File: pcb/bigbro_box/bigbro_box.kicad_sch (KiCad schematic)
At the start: 31 parts

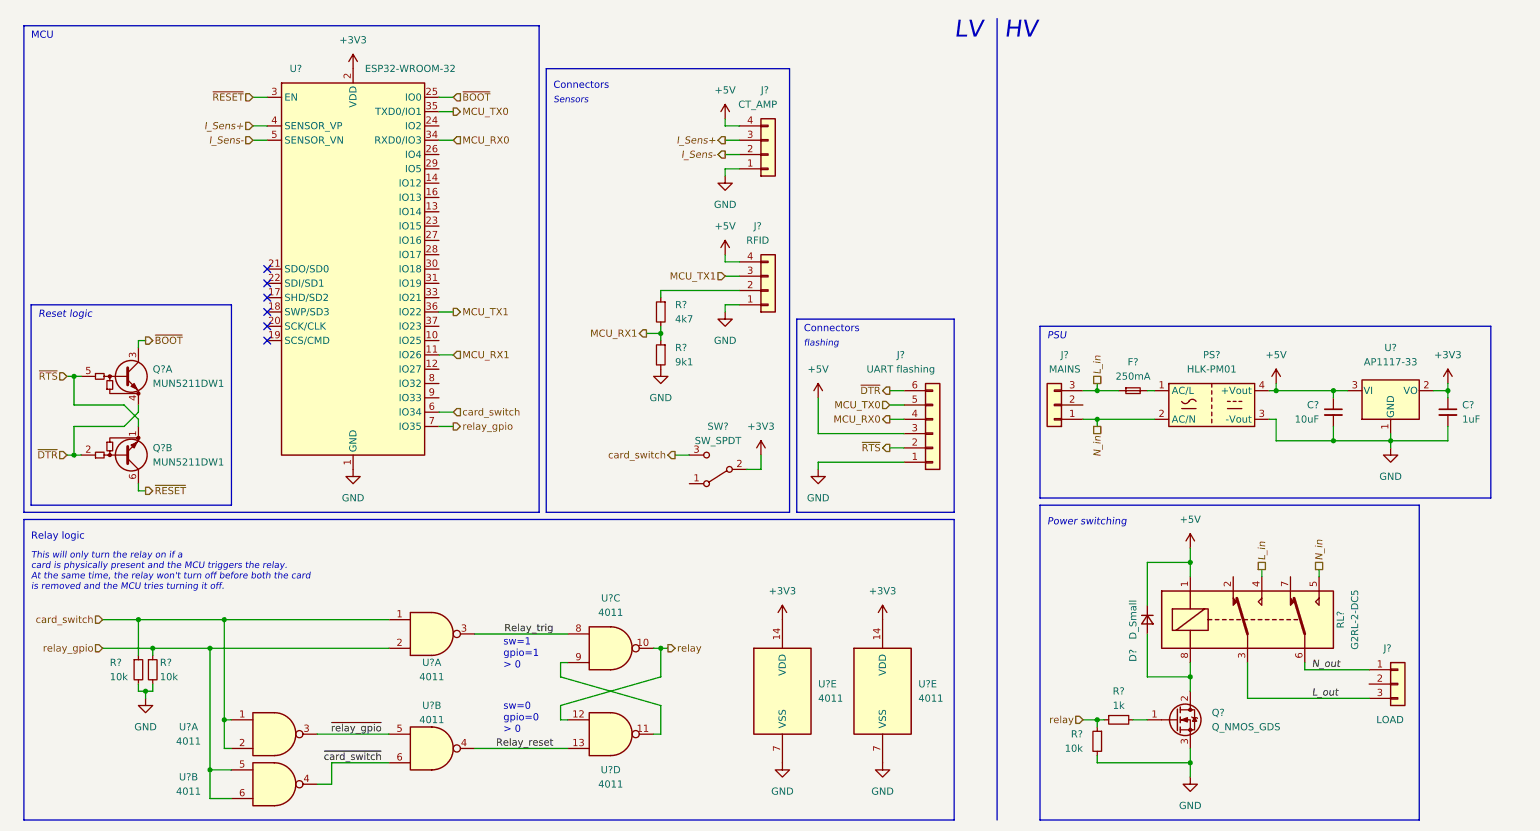
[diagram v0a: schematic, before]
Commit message: Added resistive divider to RX0
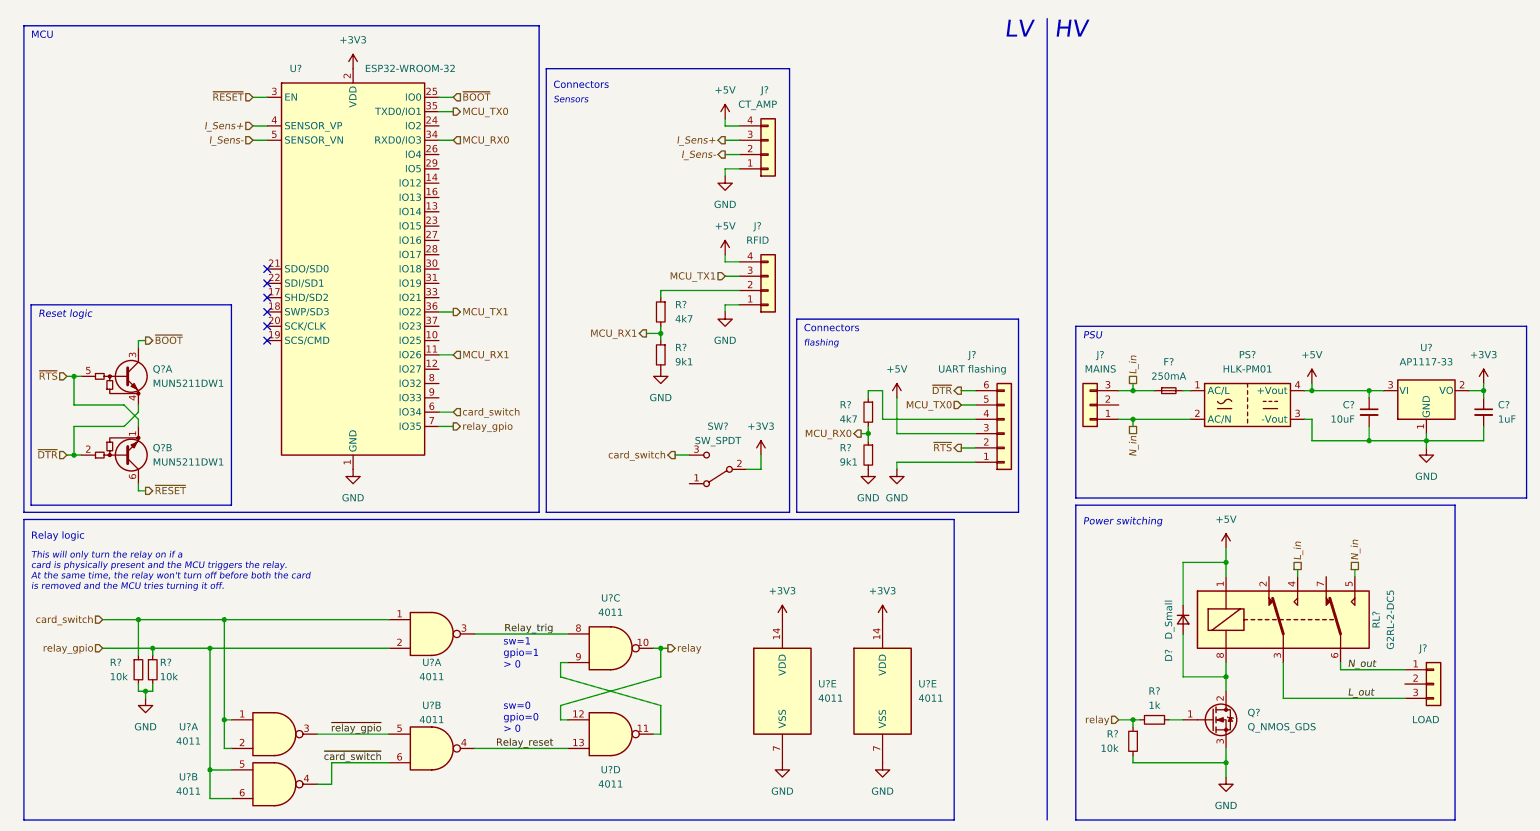
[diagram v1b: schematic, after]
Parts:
- added R?: 4k7, symbol Device:R_Small
- added R?: 9k1, symbol Device:R_Small
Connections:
- net GND: now also R?.2
- net MCU_RX0: now also R?.1, R?.2; no longer J?.4 (Pin_4)
- new net: J?.4 (Pin_4), R?.1
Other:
- moved on the sheet: C?, D?, F?, J?, PS?, Q?, R?, RL?, U?

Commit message: Moved to SPDT relay, added 24pin FPC for e-ink
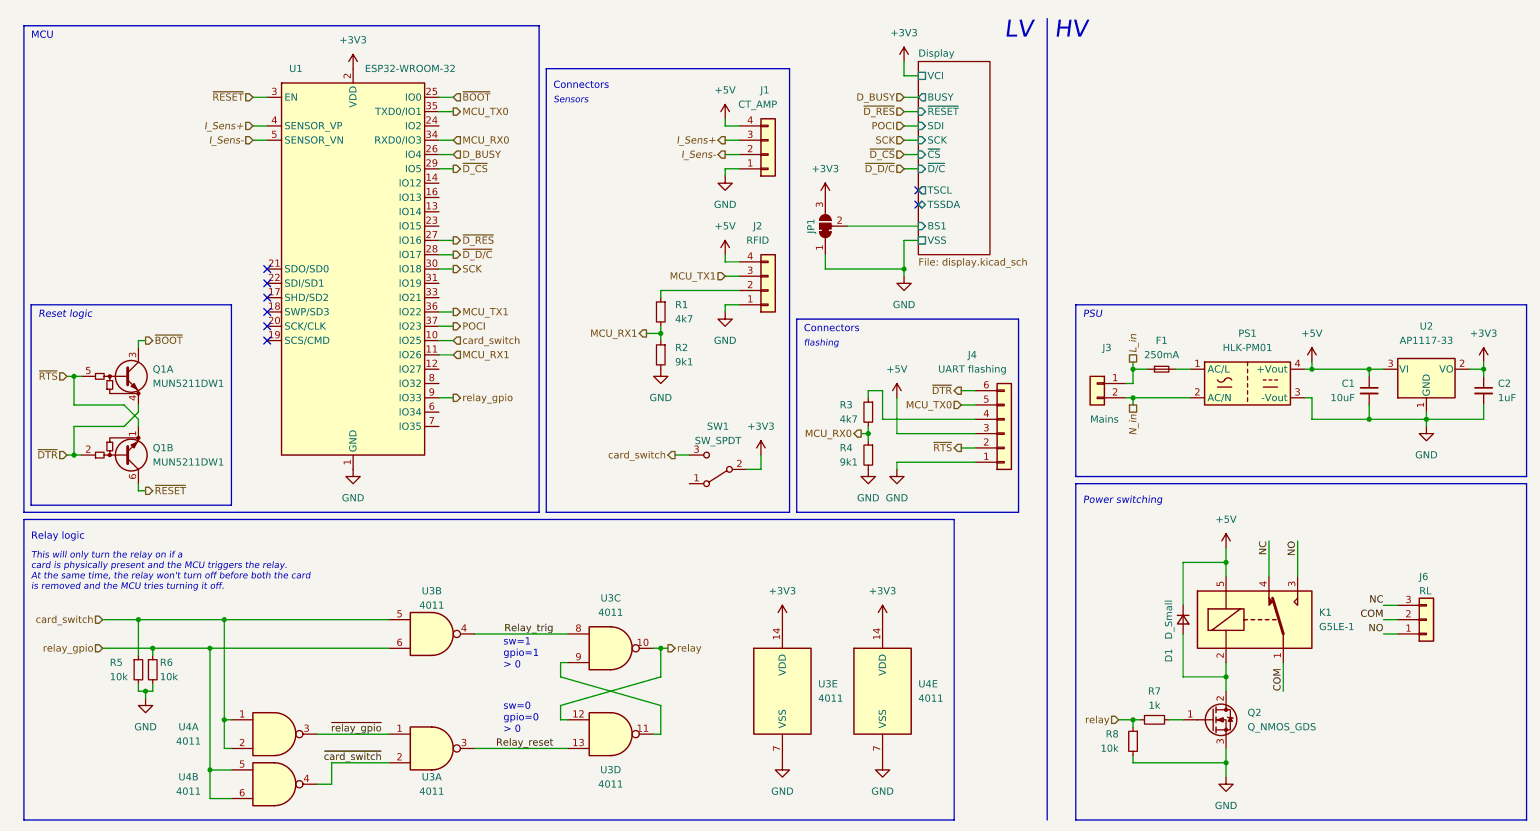
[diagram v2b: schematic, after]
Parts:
- removed J?: MAINS, symbol Connector_Generic:Conn_01x03
- removed J?: LOAD, symbol Connector_Generic:Conn_01x03
- removed RL?: G2RL-2-DC5, Relay_THT:Relay_DPDT_Omron_G2RL, symbol Relay:G2RL-2-DC5
- added J3: Mains, Connector_Phoenix_MSTB:PhoenixContact_MSTBVA_2,5_2-G-5,08_1x02_P5.08mm_Vertical, symbol Connector_Generic:Conn_01x02
- added J6: RL, Connector_Phoenix_MSTB:PhoenixContact_MSTBVA_2,5_3-G-5,08_1x03_P5.08mm_Vertical, symbol Connector_Generic:Conn_01x03
- added JP1: D_BS, Jumper:SolderJumper-3_P1.3mm_Bridged12_RoundedPad1.0x1.5mm, symbol Jumper:SolderJumper_3_Bridged12
- added K1: G5LE-1, Relay_THT:Relay_SPDT_Omron-G5LE-1, symbol Relay:G5LE-1
- C1, C2: renamed from C?; footprint (none) -> Capacitor_SMD:C_0603_1608Metric_Pad1.08x0.95mm_HandSolder
- D1: renamed from D?; footprint (none) -> Diode_SMD:D_SMA_Handsoldering
- F1: renamed from F?; footprint (none) -> Fuse:Fuseholder_Littelfuse_445_030_series_5x20mm
- J1, J2: renamed from J?; footprint (none) -> Connector_JST:JST_XH_B4B-XH-A_1x04_P2.50mm_Vertical
- J4: renamed from J?; footprint (none) -> Connector_PinHeader_2.54mm:PinHeader_1x06_P2.54mm_Vertical
- Q2: renamed from Q?; footprint (none) -> Package_TO_SOT_SMD:SOT-23_Handsoldering
- R1, R2, R3, R4, R5, R6, R7, R8: renamed from R?; footprint (none) -> Resistor_SMD:R_0603_1608Metric_Pad0.98x0.95mm_HandSolder
- SW1: renamed from SW?; footprint (none) -> Connector_JST:JST_XH_B3B-XH-A_1x03_P2.50mm_Vertical
- U3, U4: renamed from U?; footprint (none) -> Package_SO:SOIC-14_3.9x8.7mm_P1.27mm
- gave numbers to parts that had none: 4
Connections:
- net +3V3: now also JP1.3 (B)
- net +5V: now also K1.5
- net GND: now also JP1.1 (A)
- net L_in: now also J3.1 (Pin_1)
- net N_in: now also J3.2 (Pin_2)
- net Relay_reset: now also U3.3; no longer U3.4
- net Relay_trig: now also U3.4; no longer U3.3
- net card_switch: now also U1.10 (IO25), U3.5; no longer U1.6 (IO34), U3.1
- net relay_gpio: now also U1.9 (IO33), U3.6; no longer U1.7 (IO35), U3.2
- net ~{card_switch}: now also U3.2; no longer U3.6
- net ~{relay_gpio}: now also U3.1; no longer U3.5
- net at D1.2 (A), Q2.2 (D): now also K1.2
- net D_BUSY: now reaches U1.26 (IO4)
- net ~{D_RES}: now reaches U1.27 (IO16)
- net ~{D_D/C}: now reaches U1.28 (IO17)
- net ~{D_CS}: now reaches U1.29 (IO5)
- net SCK: now reaches U1.30 (IO18)
- net POCI: now reaches U1.37 (IO23)
- new net COM: J6.2 (Pin_2), K1.1
- new net Display/BS1: JP1.2 (C)
- new net NC: J6.3 (Pin_3), K1.4
- new net NO: J6.1 (Pin_1), K1.3
- no-connect marks 6 -> 8
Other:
- added sheet Display (display.kicad_sch)
- moved on the sheet: C1, C2, F1, PS1, U2, U3A, U3B

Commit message: Widened isolation slot
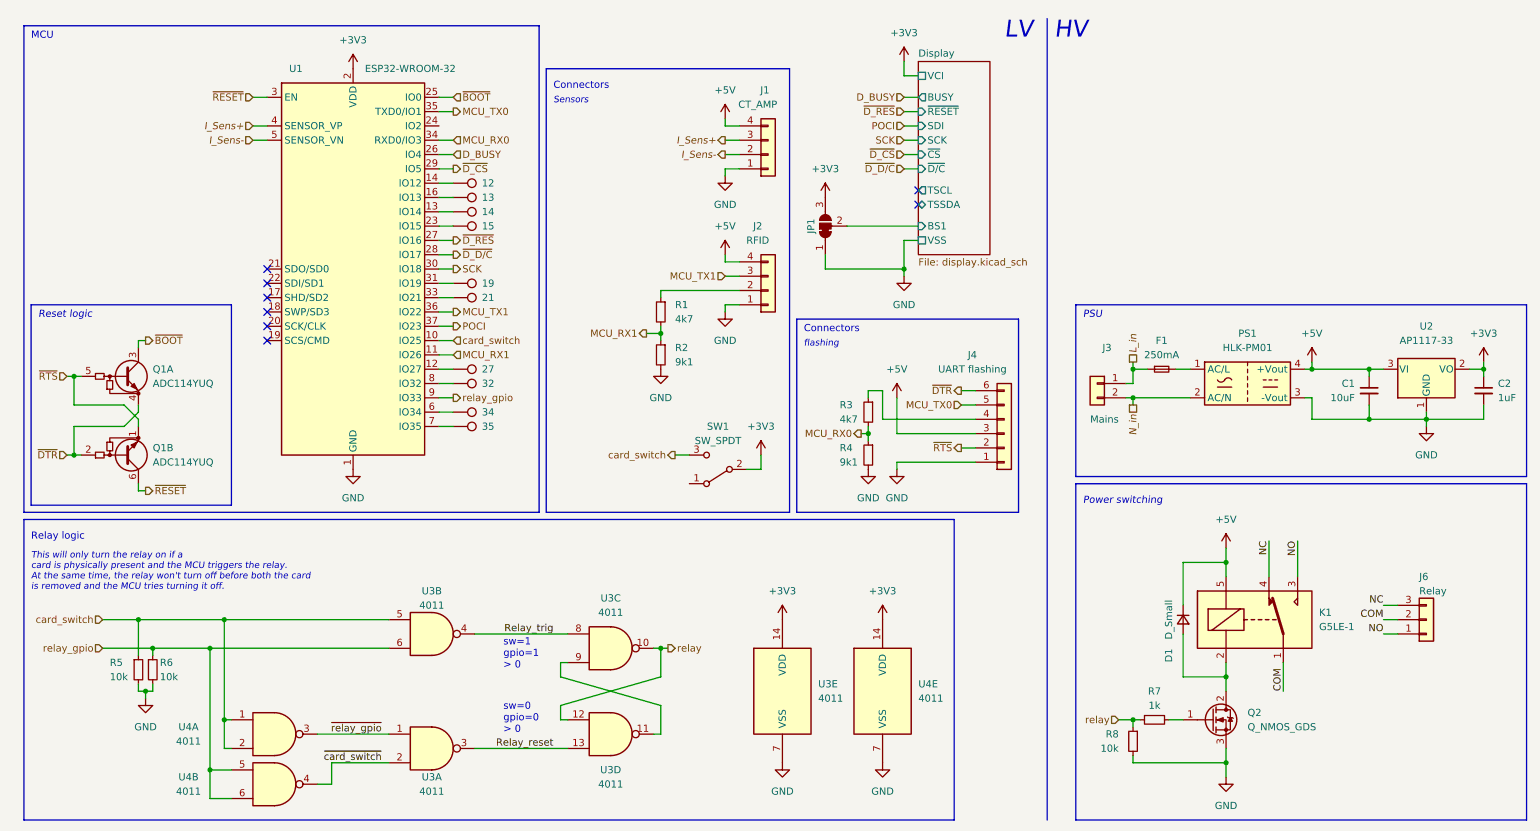
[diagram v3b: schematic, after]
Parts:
- added TP1: 12, TestPoint:TestPoint_Pad_D1.0mm, symbol Connector:TestPoint
- added TP10: 35, TestPoint:TestPoint_Pad_D1.0mm, symbol Connector:TestPoint
- added TP2: 13, TestPoint:TestPoint_Pad_D1.0mm, symbol Connector:TestPoint
- added TP3: 14, TestPoint:TestPoint_Pad_D1.0mm, symbol Connector:TestPoint
- added TP4: 15, TestPoint:TestPoint_Pad_D1.0mm, symbol Connector:TestPoint
- added TP5: 19, TestPoint:TestPoint_Pad_D1.0mm, symbol Connector:TestPoint
- added TP6: 21, TestPoint:TestPoint_Pad_D1.0mm, symbol Connector:TestPoint
- added TP7: 27, TestPoint:TestPoint_Pad_D1.0mm, symbol Connector:TestPoint
- added TP8: 32, TestPoint:TestPoint_Pad_D1.0mm, symbol Connector:TestPoint
- added TP9: 34, TestPoint:TestPoint_Pad_D1.0mm, symbol Connector:TestPoint
- D1: footprint Diode_SMD:D_SMA_Handsoldering -> Diode_SMD:D_SOD-123
- J6: value RL -> Relay
- Q1: value MUN5211DW1 -> ADC114YUQ
- Q2: footprint Package_TO_SOT_SMD:SOT-23_Handsoldering -> Package_TO_SOT_SMD:SOT-323_SC-70_Handsoldering
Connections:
- net at U1.12 (IO27): now also TP7.1
- net at U1.13 (IO14): now also TP3.1
- net at U1.14 (IO12): now also TP1.1
- net at U1.16 (IO13): now also TP2.1
- net at U1.23 (IO15): now also TP4.1
- net at U1.31 (IO19): now also TP5.1
- net at U1.33 (IO21): now also TP6.1
- net at U1.6 (IO34): now also TP9.1
- net at U1.7 (IO35): now also TP10.1
- net at U1.8 (IO32): now also TP8.1

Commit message: Order1
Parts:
- C1: value 10uF -> 1uF
- C2: value 1uF -> 10uF
- R1, R3: value 4k7 -> 1k2
- R2, R4: value 9k1 -> 2k2
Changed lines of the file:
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@@
       (effects (font (size 1.27 1.27)) (justify right))
     )
-    (property "Value" "4k7" (id 1) (at 130.81 68.5799 0)
+    (property "Value" "1k2" (id 1) (at 130.81 68.5799 0)
       (effects (font (size 1.27 1.27)) (justify right))
     )
@@
       (effects (font (size 1.27 1.27)) (justify right))
     )
-    (property "Value" "9k1" (id 1) (at 130.81 76.1999 0)
+    (property "Value" "2k2" (id 1) (at 130.81 76.1999 0)
       (effects (font (size 1.27 1.27)) (justify right))
     )
@@
       (effects (font (size 1.27 1.27)) (justify right))
     )
-    (property "Value" "4k7" (id 1) (at 160.02 86.3599 0)
+    (property "Value" "1k2" (id 1) (at 160.02 86.3599 0)
       (effects (font (size 1.27 1.27)) (justify right))
     )
@@
       (effects (font (size 1.27 1.27)) (justify right))
     )
-    (property "Value" "9k1" (id 1) (at 160.02 93.9799 0)
+    (property "Value" "2k2" (id 1) (at 160.02 93.9799 0)
       (effects (font (size 1.27 1.27)) (justify right))
     )
@@
     (pin "2")
   )
-  (symbol (lib_id "Device:C_Small") (at 254 81.28 0) (unit 1)
-    (in_bom yes) (on_board yes) (fields_autoplaced)
+  (symbol (lib_id "Device:C_Small") (at 254 81.28 0) (mirror y) (unit 1)
+    (in_bom yes) (on_board yes)
     (property "Reference" "C1" (id 0) (at 251.46 80.0099 0)
-      (effects (font (size 1.27 1.27)) (justify right))
-    )
-    (property "Value" "10uF" (id 1) (at 251.46 82.5499 0)
-      (effects (font (size 1.27 1.27)) (justify right))
+      (effects (font (size 1.27 1.27)) (justify left))
+    )
+    (property "Value" "1uF" (id 1) (at 251.46 82.5499 0)
+      (effects (font (size 1.27 1.27)) (justify left))
     )
     (property "Footprint" "Capacitor_SMD:C_0603_1608Metric_Pad1.08x0.95mm_HandSolder" (id 2) (at 254 81.28 0)
@@
       (effects (font (size 1.27 1.27)) (justify left))
     )
-    (property "Value" "1uF" (id 1) (at 276.86 82.5499 0)
+    (property "Value" "10uF" (id 1) (at 276.86 82.5499 0)
       (effects (font (size 1.27 1.27)) (justify left))
     )
@@
     )
     (path "/fbb20dfe-eb5c-4ae9-b521-0cbb2ac69fd9"
-      (reference "C1") (unit 1) (value "10uF") (footprint "Capacitor_SMD:C_0603_1608Metric_Pad1.08x0.95mm_HandSolder")
+      (reference "C1") (unit 1) (value "1uF") (footprint "Capacitor_SMD:C_0603_1608Metric_Pad1.08x0.95mm_HandSolder")
     )
     (path "/06d702a6-dac2-43ec-94bc-a9b39fb37f29"
-      (reference "C2") (unit 1) (value "1uF") (footprint "Capacitor_SMD:C_0603_1608Metric_Pad1.08x0.95mm_HandSolder")
+      (reference "C2") (unit 1) (value "10uF") (footprint "Capacitor_SMD:C_0603_1608Metric_Pad1.08x0.95mm_HandSolder")
     )
     (path "/32cbec5b-62f5-46a2-b43b-e73e9874b536/6aaa90ea-f766-449d-aeee-a8637a6e7f0c"
@@
     )
     (path "/ba86de33-da2d-4650-89b3-80cc0fb3c3d7"
-      (reference "R1") (unit 1) (value "4k7") (footprint "Resistor_SMD:R_0603_1608Metric_Pad0.98x0.95mm_HandSolder")
+      (reference "R1") (unit 1) (value "1k2") (footprint "Resistor_SMD:R_0603_1608Metric_Pad0.98x0.95mm_HandSolder")
     )
     (path "/e6bebc63-b9ab-4269-9d24-769e02bc495f"
-      (reference "R2") (unit 1) (value "9k1") (footprint "Resistor_SMD:R_0603_1608Metric_Pad0.98x0.95mm_HandSolder")
+      (reference "R2") (unit 1) (value "2k2") (footprint "Resistor_SMD:R_0603_1608Metric_Pad0.98x0.95mm_HandSolder")
     )
     (path "/3fcf8775-cc8f-4ef6-b42a-26f62cb23387"
-      (reference "R3") (unit 1) (value "4k7") (footprint "Resistor_SMD:R_0603_1608Metric_Pad0.98x0.95mm_HandSolder")
+      (reference "R3") (unit 1) (value "1k2") (footprint "Resistor_SMD:R_0603_1608Metric_Pad0.98x0.95mm_HandSolder")
     )
     (path "/dc178ce8-ddf1-4789-b3a4-5e2bce4acf7e"
-      (reference "R4") (unit 1) (value "9k1") (footprint "Resistor_SMD:R_0603_1608Metric_Pad0.98x0.95mm_HandSolder")
+      (reference "R4") (unit 1) (value "2k2") (footprint "Resistor_SMD:R_0603_1608Metric_Pad0.98x0.95mm_HandSolder")
     )
     (path "/a1e372ea-e87f-4801-b502-5aa6b244555f"
